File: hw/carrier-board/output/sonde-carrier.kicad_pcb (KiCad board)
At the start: 2 copper layers, 25 x 35 mm, 16 parts

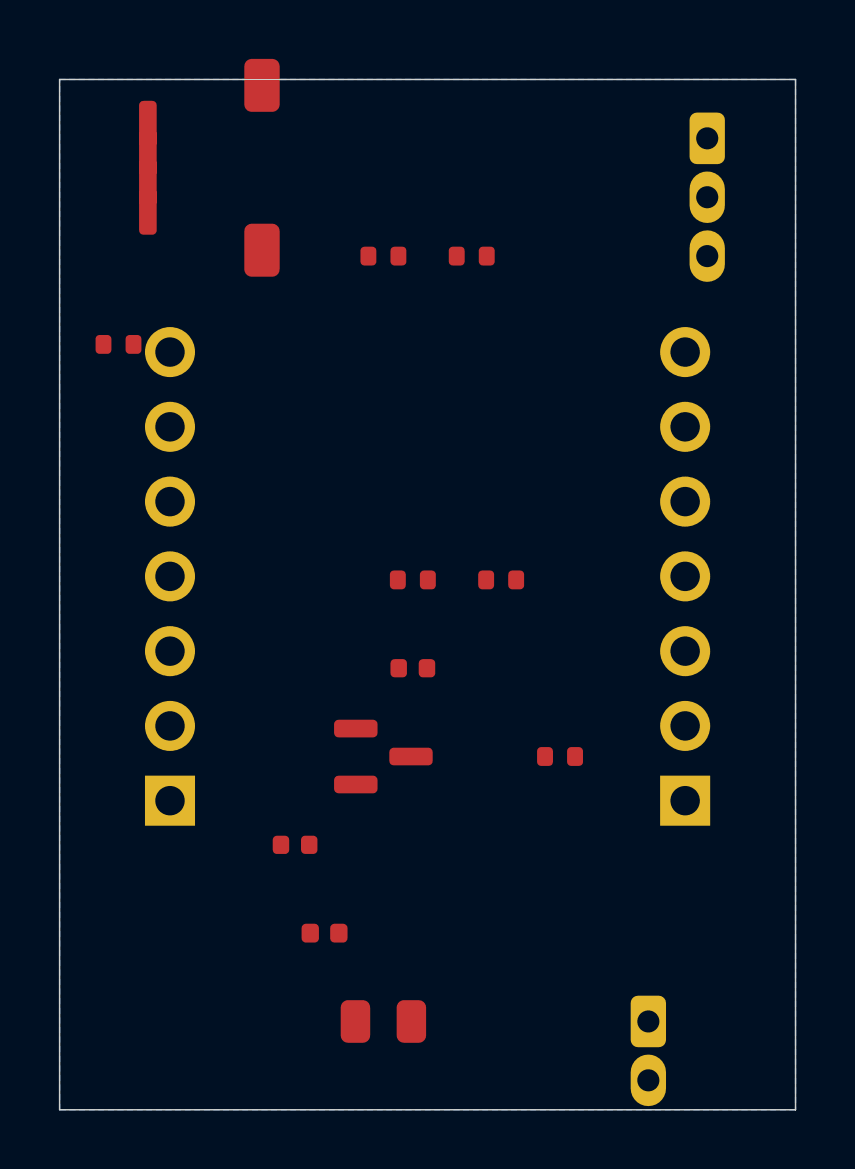
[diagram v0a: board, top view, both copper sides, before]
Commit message: feat: hand-routed carrier board PCB — 0 unconnected, 21 DRC (inherent)
Manually routed all 9 signal nets on the sonde carrier board:
- VBAT, VBAT_FILT (0.5mm power traces)
- SENSOR_V (0.3mm power trace)
- SENSOR_EN, SDA, SCL, 1W_DATA, VBAT_SENSE (0.25mm signals)
- GND via B.Cu copper pour with vias

DRC: 21 violations (15 lib_footprint_mismatch + 6 solder_mask_bridge)
ERC: 0 violations
Unconnected: 0

Co-authored-by: Copilot <223556219+Copilot@users.noreply.github.com>
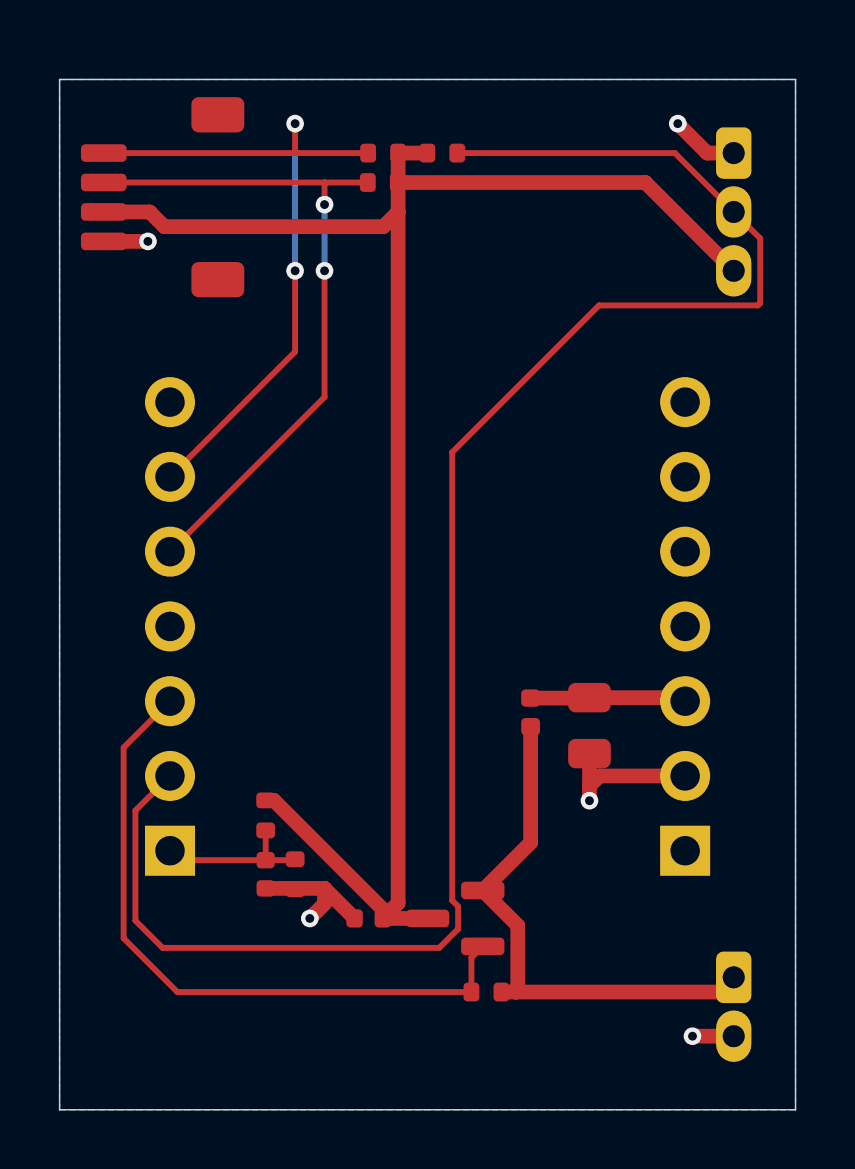
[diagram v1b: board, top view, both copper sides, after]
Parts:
- moved R3 12.8 mm to (149.0, 90.0), turned to 180 degrees
- moved C1 12.2 mm to (154.0, 109.5), turned to -90 degrees
- moved R6 12.2 mm to (144.0, 114.5), turned to -90 degrees
- moved FB1 10.3 mm to (152.0, 109.0), turned to 90 degrees
- moved R5 9.43 mm to (143.0, 112.5), turned to -90 degrees
- moved C3 8.60 mm to (143.0, 114.5), turned to -90 degrees
- moved R4 8.38 mm to (150.5, 118.5)
- moved Q1 6.02 mm to (149.4, 116.0), turned to 180 degrees
- moved R2 4.62 mm to (147.0, 90.0)
- moved C2 3.54 mm to (146.5, 116.0), turned to 180 degrees
- moved J3 3.26 mm to (158.9, 118.0)
- moved R1 2.50 mm to (147.0, 91.0)
- moved J1 1.80 mm to (139.5, 91.5)
- moved J6 1.70 mm to (139.8, 113.7)
- moved J7 1.70 mm to (157.2, 113.7)
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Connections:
- J6 pad 7: VBAT_FILT -> (no net)
- J7 pad 2: (no net) -> GND
- J7 pad 3: (no net) -> VBAT_FILT
- J7 pad 6: GND -> (no net)
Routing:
- net 1W_DATA: track 0.00 -> 59.5 mm
- net SENSOR_V: track 0.00 -> 57.6 mm
- net SCL: track 0.00 -> 23.7 mm, vias 0 -> 2
- net SDA: track 0.00 -> 23.7 mm, vias 0 -> 2
- net SENSOR_EN: track 0.00 -> 23.0 mm
- net VBAT: track 0.00 -> 18.3 mm
- net GND: track 0.00 -> 14.9 mm, vias 0 -> 5
- net VBAT_SENSE: track 0.00 -> 5.40 mm
- net VBAT_FILT: track 0.00 -> 5.31 mm
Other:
- board text added: "+ -"
- board text added: "sonde rev_a"
- board text removed: "+ −"
- board text removed: "sonde"
